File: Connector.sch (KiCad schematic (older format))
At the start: 3 parts

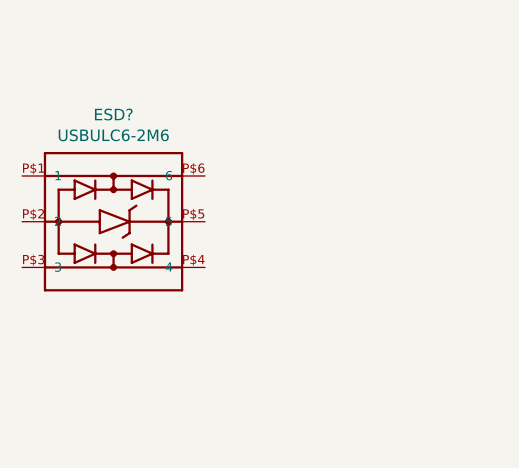
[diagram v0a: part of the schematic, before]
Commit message: Added all ICs expcept Power supply
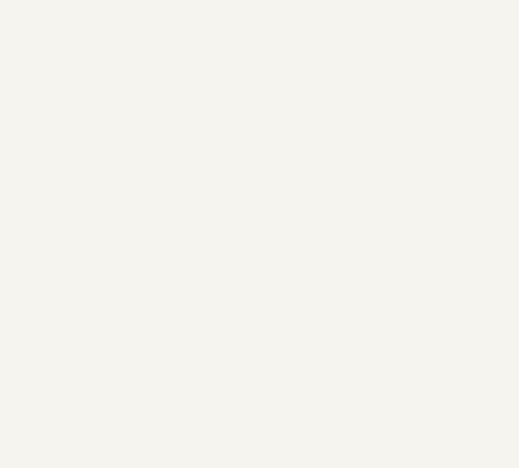
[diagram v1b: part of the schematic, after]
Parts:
- removed ESD?: USBULC6-2M6, UQFN6, symbol USBULC6-2M6:USBULC6-2M6
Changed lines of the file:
@@
-$EndComp
-$Comp
-L USBULC6-2M6:USBULC6-2M6 ESD?
-U 1 1 5FB04B58
-P 5450 2100
-AR Path="/5FB04B58" Ref="ESD?"  Part="1"
-AR Path="/5FAAF61E/5FB04B58" Ref="ESD?"  Part="1"
-F 0 "ESD?" H 5450 2567 50  0000 C CNN
-F 1 "USBULC6-2M6" H 5450 2476 50  0000 C CNN
-F 2 "UQFN6" H 5450 2100 50  0001 L BNN
-F 3 "" H 5450 2100 50  0001 L BNN
-F 4 "Unavailable" H 5450 2100 50  0001 L BNN "Field4"
-F 5 "USBULC6-2M6" H 5450 2100 50  0001 L BNN "Field5"
-F 6 "USBULC6 Series 6 V 2 Channel SMT Bi-Directional ESD Protection - UQFN-6" H 5450 2100 50  0001 L BNN "Field6"
-F 7 "UFDFN-6 STMicroelectronics" H 5450 2100 50  0001 L BNN "Field7"
-F 8 "None" H 5450 2100 50  0001 L BNN "Field8"
-	1    5450 2100
-	1    0    0    -1
 $EndComp
 $Comp
